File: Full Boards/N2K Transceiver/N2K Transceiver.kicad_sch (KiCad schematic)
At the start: 75 parts, among them J1 Optional Bond, J3 JTAG, SW1 SW_MEC_5G, SW2 SW_MEC_5G, SW3 SW_MEC_5G

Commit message: Added a DNP capacitor and resistor to the MCU in case testing shows hot plugging going above 40V.
Signed-off-by: digimer <digital.mermaid@gmail.com>
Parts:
- removed R27: 1kR, mr-stuff:Stackpole RNCP0805, symbol mr-parts:Stackpole RNCP0805FTD1K00
- added C5: 330uF, mr-stuff:Panasonic EEH-ZU, symbol mr-parts:Panasonic EEH-ZU
- added R27: 0.2mR, mr-stuff:KOA SR73, symbol mr-parts:KOA Speer SR732BTTDR200F
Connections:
- net +3.3V: now also R27.2
- net GND: now also C5.2
- net MCU_RESET: no longer names the net of C14.1, MCU1.3 (EN), R3.1, SW1.3 (B), SW1.4 (B)
- net MCU_RESET: no longer MCU1.20 (IO12)
- new net: C5.1, R27.1
- no-connect marks 9 -> 11
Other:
- moved on the sheet: C10, C11, C12

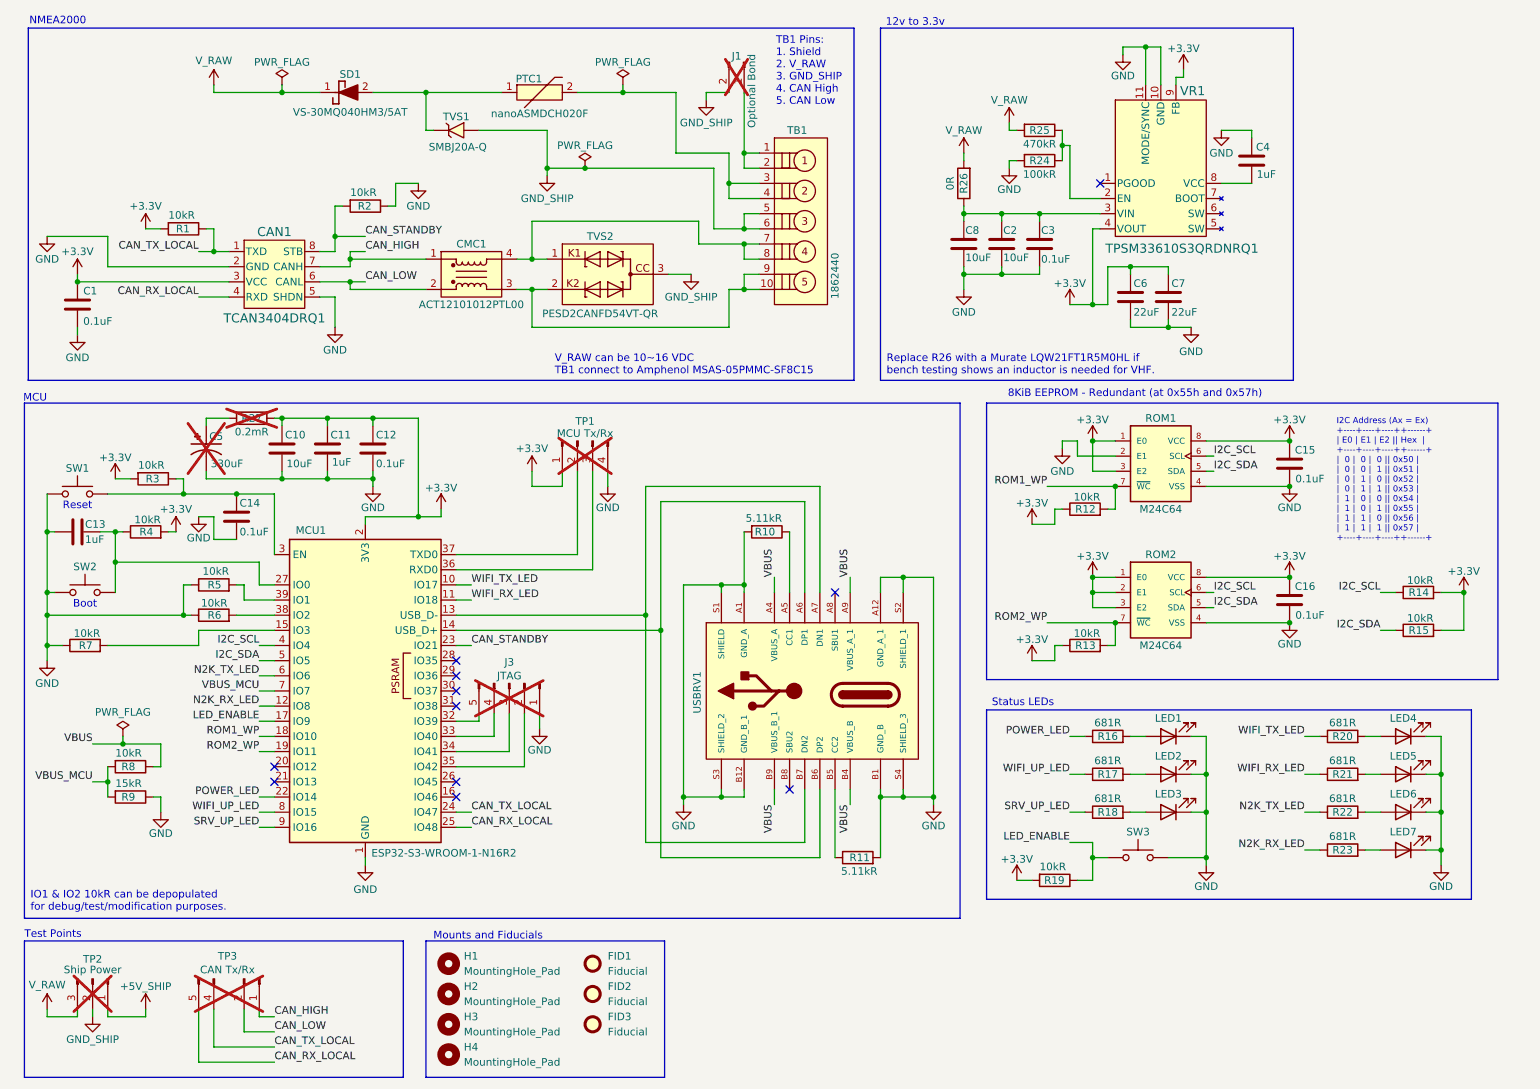
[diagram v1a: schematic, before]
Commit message: Moved the RC circuit to VR1 where it should have been. Removed the old TP2.
Signed-off-by: digimer <digital.mermaid@gmail.com>
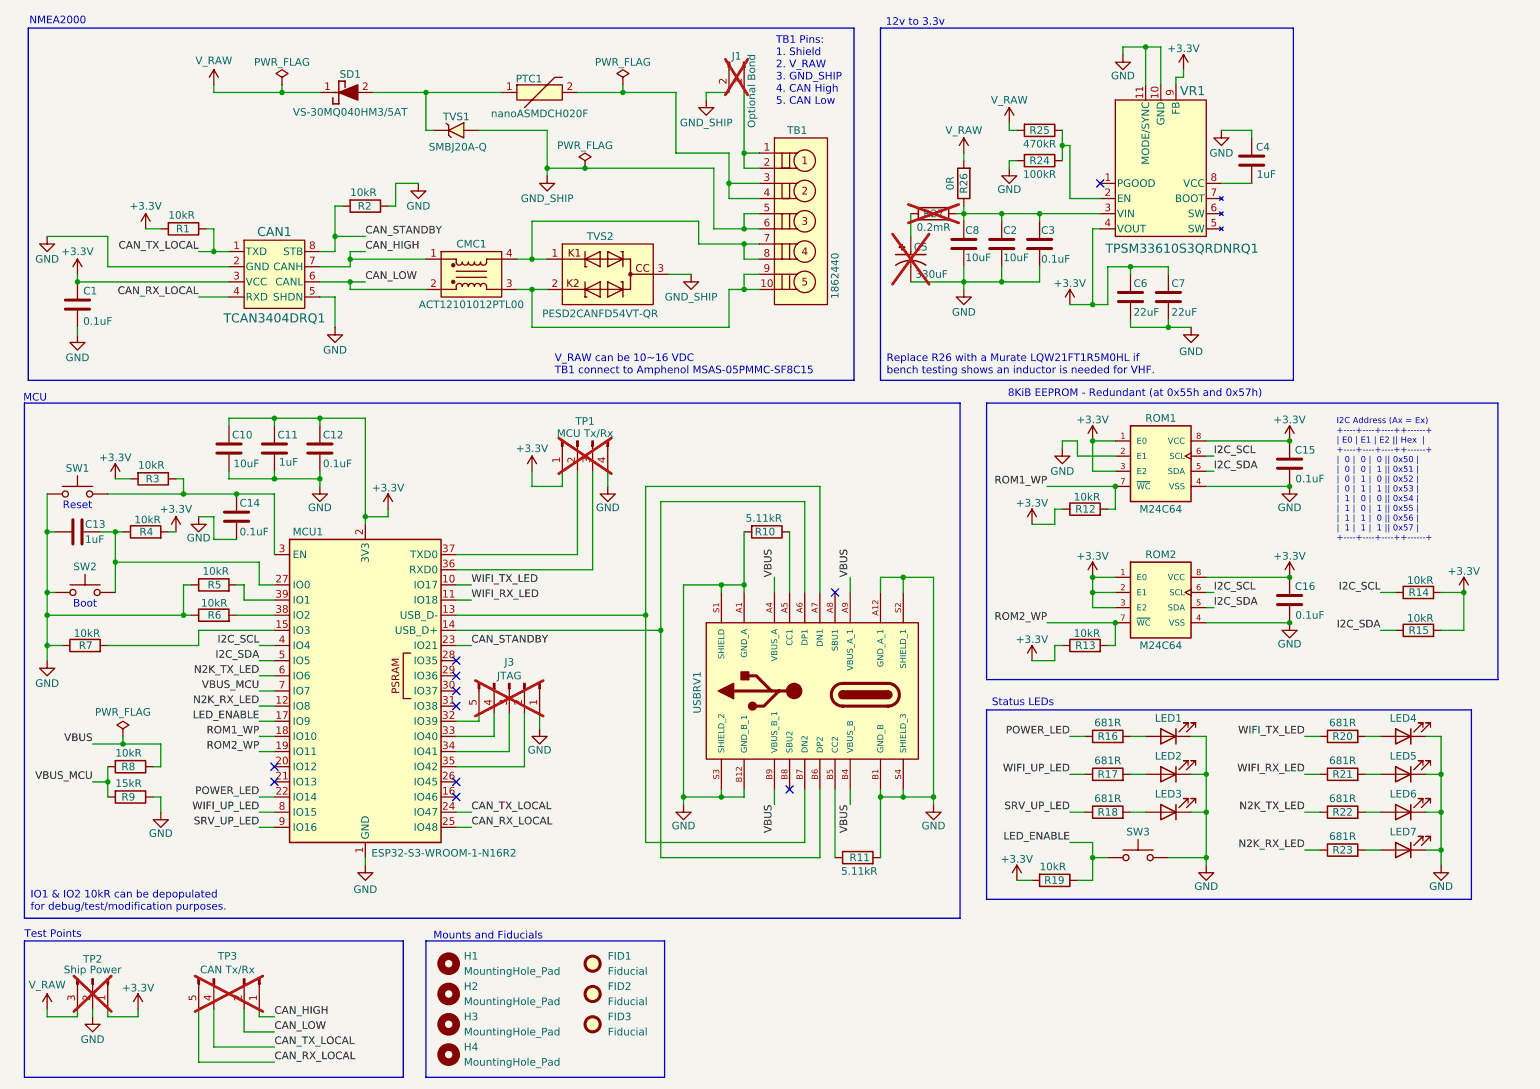
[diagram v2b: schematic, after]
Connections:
- net +5V_SHIP is gone; now on net +3.3V: TP2.1 (Pin_1)
- net +3.3V: no longer R27.2
- net GND: now also TP2.2 (Pin_2)
- net GND_SHIP: no longer TP2.2 (Pin_2)
- net at C2.1, C3.1, C8.1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: now also R27.2
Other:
- moved on the sheet: C10, C11, C12

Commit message: Removed remaining GND_SHIP references and removed the shield to ground option.
Signed-off-by: digimer <digital.mermaid@gmail.com>
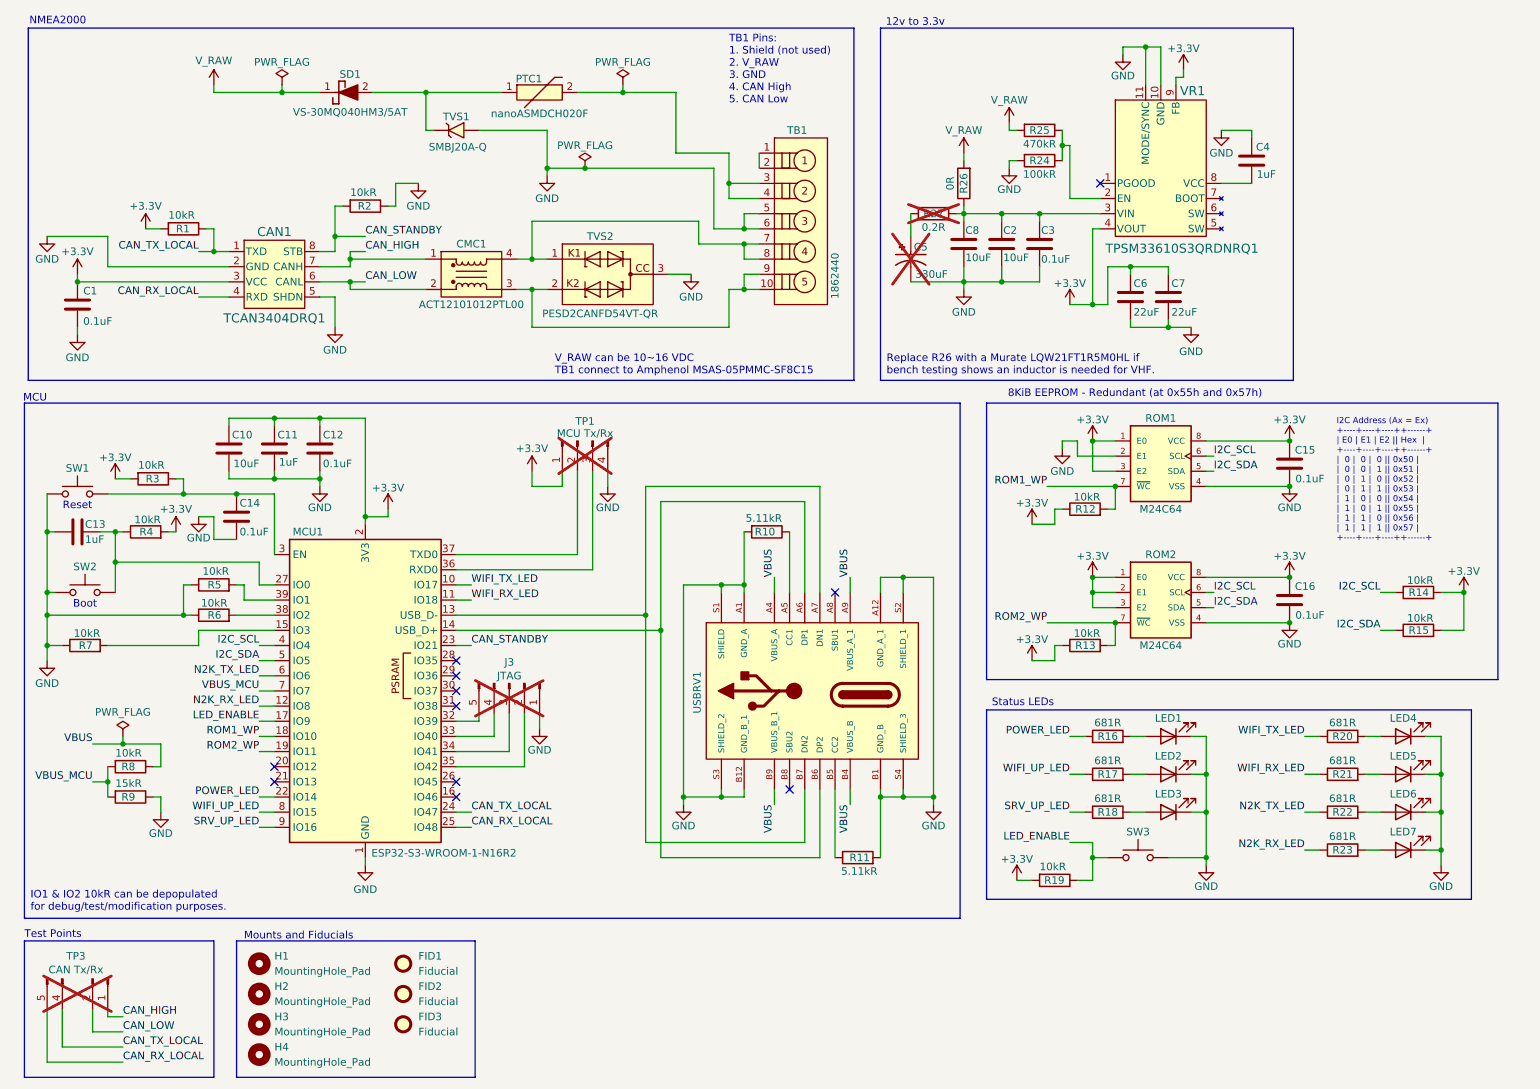
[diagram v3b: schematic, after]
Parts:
- removed J1: Optional Bond, Connector_PinHeader_2.54mm:PinHeader_1x02_P2.54mm_Vertical, symbol Connector:Conn_01x02_Pin
- removed TP2: Ship Power, Connector_PinHeader_2.54mm:PinHeader_1x03_P2.54mm_Vertical, symbol Connector:Conn_01x03_Pin
- R27: value 0.2mR -> 0.2R
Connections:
- net GND_SHIP is gone; now on net GND: TB1.5, TB1.6, TVS1.2 (A), TVS2.3
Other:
- note added: "TB1 Pins: 1. Shield (not used) 2. V_RAW 3. GND 4. CAN High 5. CAN Low"
- note removed: "TB1 Pins: 1. Shield 2. V_RAW 3. GND_SHIP 4. CAN High 5. CAN Low"
- moved on the sheet: FID1, FID2, FID3, H1, H2, H3, H4, TP3

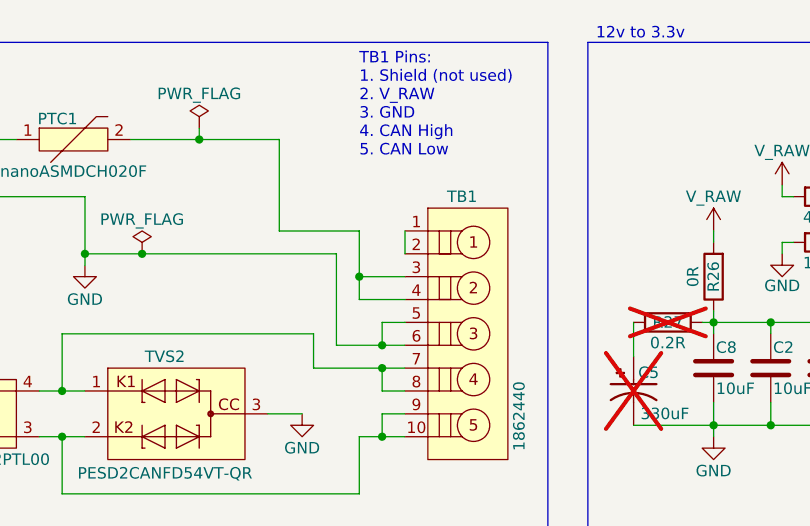
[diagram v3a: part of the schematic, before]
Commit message: Removed the isolated link between TB1 pins 1 and 2.
Signed-off-by: digimer <digital.mermaid@gmail.com>
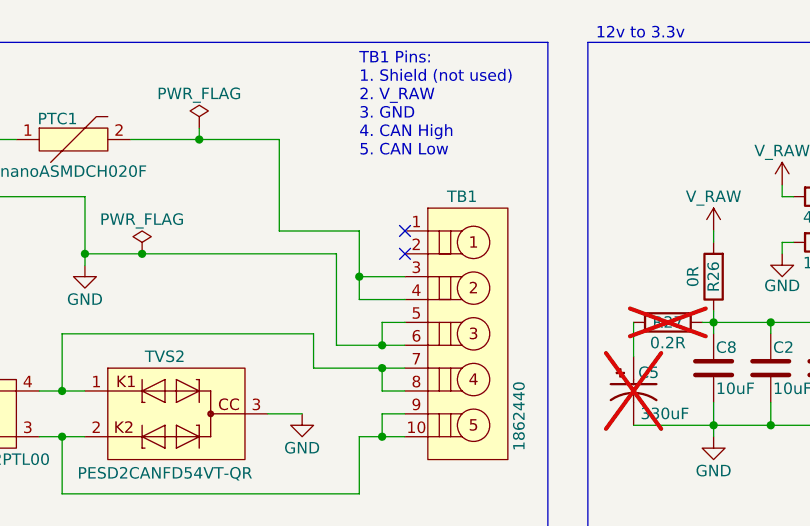
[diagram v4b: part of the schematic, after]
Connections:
- net at TB1.1: no longer TB1.2
- no-connect marks 11 -> 13
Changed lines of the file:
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@@
+	)
+	(no_connect
+		(at 138.43 36.83)
+	)
+	(no_connect
+		(at 138.43 39.37)
 	)
 	(no_connect
@@
 		)
 		(stroke
-			(width 0)
-			(type default)
-		)
-	)
-	(wire
-		(pts
-			(xy 138.43 36.83) (xy 138.43 39.37)
-		)
-		(stroke

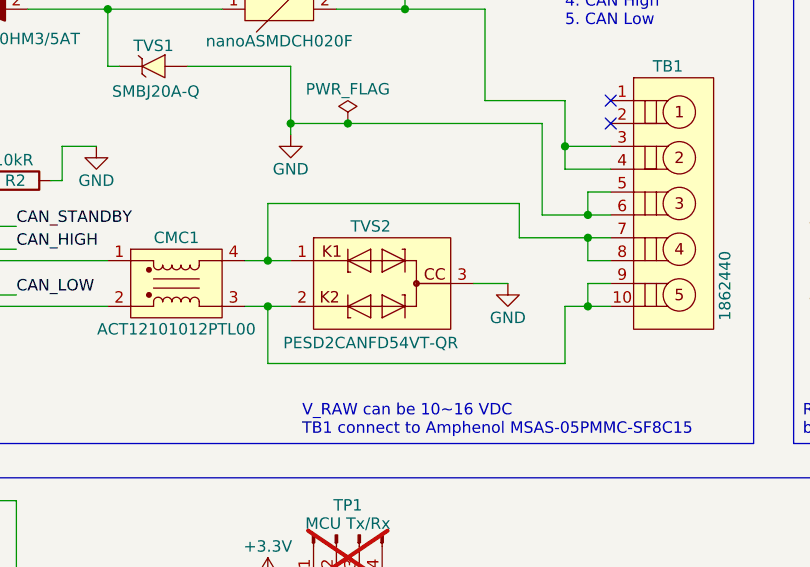
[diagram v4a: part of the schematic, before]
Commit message: Updated the TVS2 (CAN bus) to a Vishay VCAN33A2-03SHE3A08.
Signed-off-by: digimer <digital.mermaid@gmail.com>
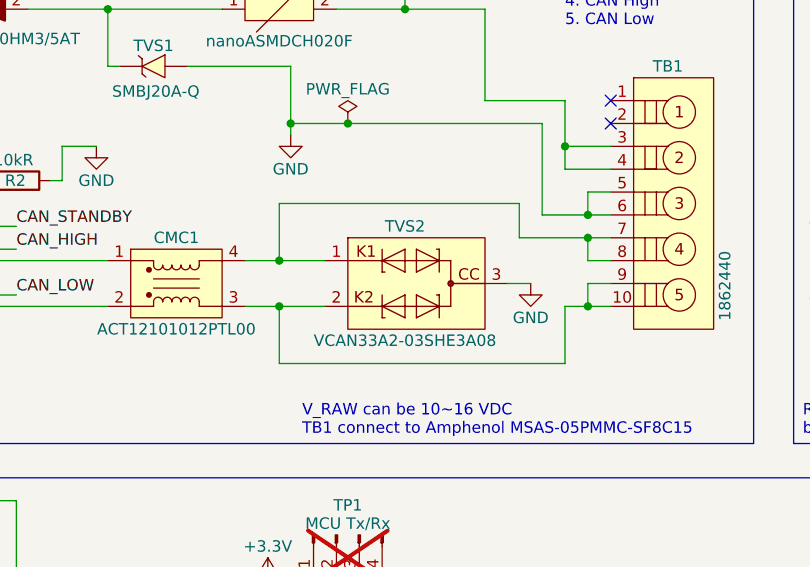
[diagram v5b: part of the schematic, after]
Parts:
- removed TVS2: PESD2CANFD54VT-QR, mr-stuff:Nexperia PESD2CANFD, symbol mr-parts:Nexperia PESD2CANFD54VT-QR
- added TVS2: VCAN33A2-03SHE3A08, symbol mr-parts:Vishay VCAN33A2-03SHE3A08
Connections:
- net GND: now also TVS2.3
- net at CMC1.4 (O1), TB1.7, TB1.8: now also TVS2.1
- net at CMC1.3 (O2), TB1.10, TB1.9: now also TVS2.2
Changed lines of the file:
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@@
 	)
 	(junction
+		(at 101.6 59.69)
+		(diameter 0)
+		(color 0 0 0 0)
+	)
+	(junction
 		(at 162.56 144.78)
 		(diameter 0)
@@
 	)
 	(junction
-		(at 100.33 54.61)
-		(diameter 0)
-		(color 0 0 0 0)
-	)
-	(junction
 		(at 167.64 144.78)
 		(diameter 0)
@@
 	)
 	(junction
-		(at 19.05 110.49)
+		(at 101.6 54.61)
 		(diameter 0)
 		(color 0 0 0 0)
 	)
 	(junction
-		(at 100.33 59.69)
+		(at 19.05 110.49)
 		(diameter 0)
 		(color 0 0 0 0)
@@
 	(wire
 		(pts
-			(xy 100.33 59.69) (xy 102.87 59.69)
-		)
-		(stroke
-			(width 0)
-			(type default)
-		)
-	)
-	(wire
-		(pts
 			(xy 44.45 116.84) (xy 44.45 119.38)
 		)
@@
 	(wire
 		(pts
-			(xy 100.33 59.69) (xy 100.33 66.04)
+			(xy 101.6 59.69) (xy 101.6 66.04)
 		)
 		(stroke
@@
 	(wire
 		(pts
+			(xy 101.6 54.61) (xy 106.68 54.61)
+		)
+		(stroke
+			(width 0)
+			(type default)
+		)
+	)
+	(wire
+		(pts
 			(xy 99.06 139.7) (xy 87.63 139.7)
 		)
@@
 	(wire
 		(pts
+			(xy 101.6 59.69) (xy 106.68 59.69)
+		)
+		(stroke
+			(width 0)
+			(type default)
+		)
+	)
+	(wire
+		(pts
 			(xy 162.56 144.78) (xy 162.56 143.51)
 		)
@@
 	(wire
 		(pts
-			(xy 100.33 54.61) (xy 100.33 48.26)
+			(xy 101.6 54.61) (xy 101.6 48.26)
 		)
 		(stroke
@@
 	(wire
 		(pts
-			(xy 97.79 54.61) (xy 100.33 54.61)
+			(xy 97.79 54.61) (xy 101.6 54.61)
 		)
 		(stroke
@@
 	(wire
 		(pts
-			(xy 100.33 66.04) (xy 133.35 66.04)
+			(xy 101.6 66.04) (xy 133.35 66.04)
 		)
 		(stroke
@@
 	(wire
 		(pts
-			(xy 100.33 54.61) (xy 102.87 54.61)
-		)
-		(stroke
-			(width 0)
-			(type default)
-		)
-	)
-	(wire
-		(pts
 			(xy 148.59 92.71) (xy 148.59 110.49)
 		)
@@
 	(wire
 		(pts
-			(xy 100.33 48.26) (xy 128.27 48.26)
+			(xy 101.6 48.26) (xy 128.27 48.26)
 		)
 		(stroke
@@
 	(wire
 		(pts
-			(xy 127 57.15) (xy 123.19 57.15)
+			(xy 129.54 57.15) (xy 127 57.15)
 		)
 		(stroke
@@
 	(wire
 		(pts
-			(xy 97.79 59.69) (xy 100.33 59.69)
+			(xy 97.79 59.69) (xy 101.6 59.69)
 		)
 		(stroke
@@
 	)
 	(symbol
-		(lib_id "mr-parts:Nexperia PESD2CANFD54VT-QR")
-		(at 111.76 57.15 0)
-		(unit 1)
-		(body_style 1)
-		(exclude_from_sim no)
-		(in_bom yes)
-		(on_board yes)
-		(in_pos_files yes)
-		(dnp no)
-		(property "Reference" "TVS2"
-			(at 111.76 50.8 0)
-			(show_name no)
-			(do_not_autoplace no)
-			(effects
-				(font
-					(size 1.27 1.27)
-				)
-			)
-		)
-		(property "Value" "PESD2CANFD54VT-QR"
-			(at 111.76 63.754 0)
-			(show_name no)
-			(do_not_autoplace no)
-			(effects
-				(font
-					(size 1.27 1.27)
-				)
-			)
-		)
-		(property "Footprint" "mr-stuff:Nexperia PESD2CANFD"
-			(at 156.21 152.07 0)
-			(hide yes)
-			(show_name no)
-			(do_not_autoplace no)
-			(effects
-				(font
-					(size 1.27 1.27)
-				)
-				(justify left top)
-			)
-		)
-		(property "Datasheet" "https://assets.nexperia.com/documents/data-sheet/PESD2CANFD54VT-Q.pdf"
-			(at 156.21 252.07 0)
-			(hide yes)
-			(show_name no)
-			(do_not_autoplace no)
-			(effects
-				(font
-					(size 1.27 1.27)
-				)
-				(justify left top)
-			)
-		)
-		(property "Description" "41V Clamp 5A (8/20s) Ip EsD Diode Surface Mount TO-236AB ,24V (Max) 41V .-55C ~ 150C (TA)"
-			(at 111.76 67.31 0)
-			(hide yes)
-			(show_name no)
-			(do_not_autoplace no)
-			(effects
-				(font
-					(size 1.27 1.27)
-				)
-			)
-		)
-		(property "Part" "Nexperia PESD2CANFD54VT-QR"
-			(at 156.21 652.07 0)
-			(hide yes)
-			(show_name no)
-			(do_not_autoplace no)
-			(effects
-				(font
-					(size 1.27 1.27)
-				)
-				(justify left top)
-			)
-		)
-		(pin "3"
-		)
-		(pin "2"
-		)
-		(pin "1"
-		)
-		(instances
-			(project "N2K Transceiver"
-				(path "/2a070473-cb6e-4844-8f2a-5ea6a35ddb49"
-					(reference "TVS2")
-					(unit 1)
-				)
-			)
-		)
-	)
-	(symbol
 		(lib_id "Device:R")
 		(at 46.99 109.22 90)
@@
 	(symbol
 		(lib_id "power:GND")
-		(at 127 57.15 0)
+		(at 129.54 57.15 0)
 		(unit 1)
 		(body_style 1)
@@
 		(dnp no)
 		(property "Reference" "#PWR0118"
-			(at 127 63.5 0)
+			(at 129.54 63.5 0)
 			(hide yes)
 			(show_name no)
@@
 		)
 		(property "Value" "GND"
-			(at 127 60.96 0)
+			(at 129.54 60.96 0)
 			(show_name no)
 			(do_not_autoplace no)
@@
 		)
 		(property "Footprint" ""
-			(at 127 57.15 0)
+			(at 129.54 57.15 0)
 			(hide yes)
 			(show_name no)
@@
 		)
 		(property "Datasheet" ""
-			(at 127 57.15 0)
+			(at 129.54 57.15 0)
 			(hide yes)
 			(show_name no)
@@
 		)
 		(property "Description" "Power symbol creates a global label with name \"GND\" , ground"
-			(at 127 57.15 0)
+			(at 129.54 57.15 0)
 			(hide yes)
 			(show_name no)
@@
 					(unit 1)
 				)
+			)
+		)
+	)
+	(symbol
+		(lib_id "mr-parts:Vishay VCAN33A2-03SHE3A08")
+		(at 115.57 57.15 0)
+		(unit 1)
+		(body_style 1)
+		(exclude_from_sim no)
+		(in_bom yes)
+		(on_board yes)
+		(in_pos_files yes)
+		(dnp no)
+		(property "Reference" "TVS2"
+			(at 115.57 50.8 0)
+			(show_name no)
+			(do_not_autoplace no)
+			(effects
+				(font
+					(size 1.27 1.27)
+				)
+			)
+		)
+		(property "Value" "VCAN33A2-03SHE3A08"
+			(at 115.57 63.5 0)
+			(show_name no)
+			(do_not_autoplace no)
+			(effects
+				(font
+					(size 1.27 1.27)
+				)
+			)
+		)
+		(property "Footprint" ""
+			(at 160.02 152.07 0)
+			(hide yes)
+			(show_name no)
+			(do_not_autoplace no)
+			(effects
+				(font
+					(size 1.27 1.27)
+				)
+				(justify left top)
+			)
+		)
+		(property "Datasheet" "https://www.vishay.com/docs/86323/vcan33a2-03s.pdf"
+			(at 160.02 252.07 0)
+			(hide yes)
+			(show_name no)
+			(do_not_autoplace no)
+			(effects
+				(font
+					(size 1.27 1.27)
+				)
+				(justify left top)
+			)
+		)
+		(property "Description" "56V Clamp 2.7A (8/20µs) Ipp Tvs Diode Surface Mount SOT-23-3"
+			(at 115.57 67.31 0)
+			(hide yes)
+			(show_name no)
+			(do_not_autoplace no)
+			(effects
+				(font
+					(size 1.27 1.27)
+				)
+			)
+		)
+		(property "Part" "Vishay VCAN33A2-03SHE3A08"
+			(at 160.02 652.07 0)
+			(hide yes)
+			(show_name no)
+			(do_not_autoplace no)
+			(effects
+				(font
+					(size 1.27 1.27)
+				)
+				(justify left top)
+			)
+		)
+		(pin "2"
+		)
+		(pin "3"
+		)
+		(pin "1"
+		)
+		(instances
+			(project "N2K Transceiver"
+				(path "/2a070473-cb6e-4844-8f2a-5ea6a35ddb49"
+					(reference "TVS2")
+					(unit 1)
+				)
